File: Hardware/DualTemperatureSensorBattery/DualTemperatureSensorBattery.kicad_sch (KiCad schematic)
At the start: 22 parts, among them J2 Conn_01x06, Q101 BSS84, SW2 SW_Push, U1 ME54BS01_V1.0

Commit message: Rename the project. Finish routing.
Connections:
- net Enable-Battery: now also U1.8 (P1.06/AIN2); no longer U1.7 (P1.14/AIN7)
- net PROBE_1_DIVIDER: now also U1.4 (P1.11/AIN4); no longer U1.5 (P1.12/AIN5)
- net PROBE_2_DIVIDER: now also U1.5 (P1.12/AIN5); no longer U1.4 (P1.11/AIN4)
- net VDD: no longer J2.6 (Pin_6)
- net V_{BAT}: now also U1.7 (P1.14/AIN7); no longer U1.8 (P1.06/AIN2)
- net +BATT: now reaches BT1.1 (+), C6.1, JP1.1 (A), Probe3.1 (Pin_1)
- net +BATT: now also J2.6 (Pin_6)

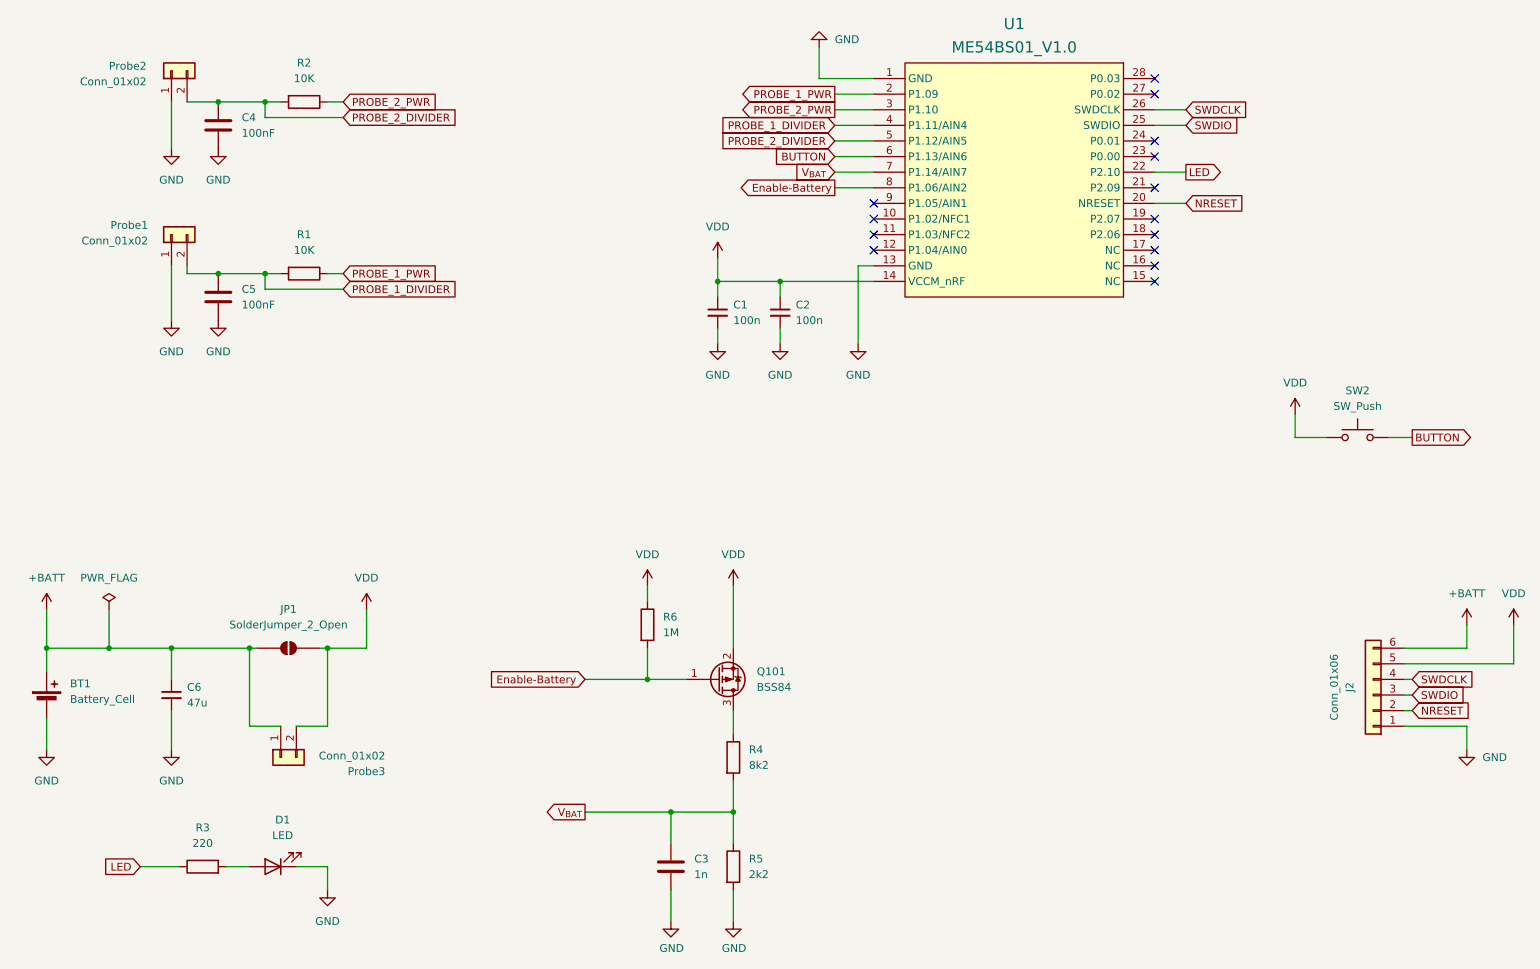
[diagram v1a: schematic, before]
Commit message: Removed the battery measurement. Reworked some of the layout.
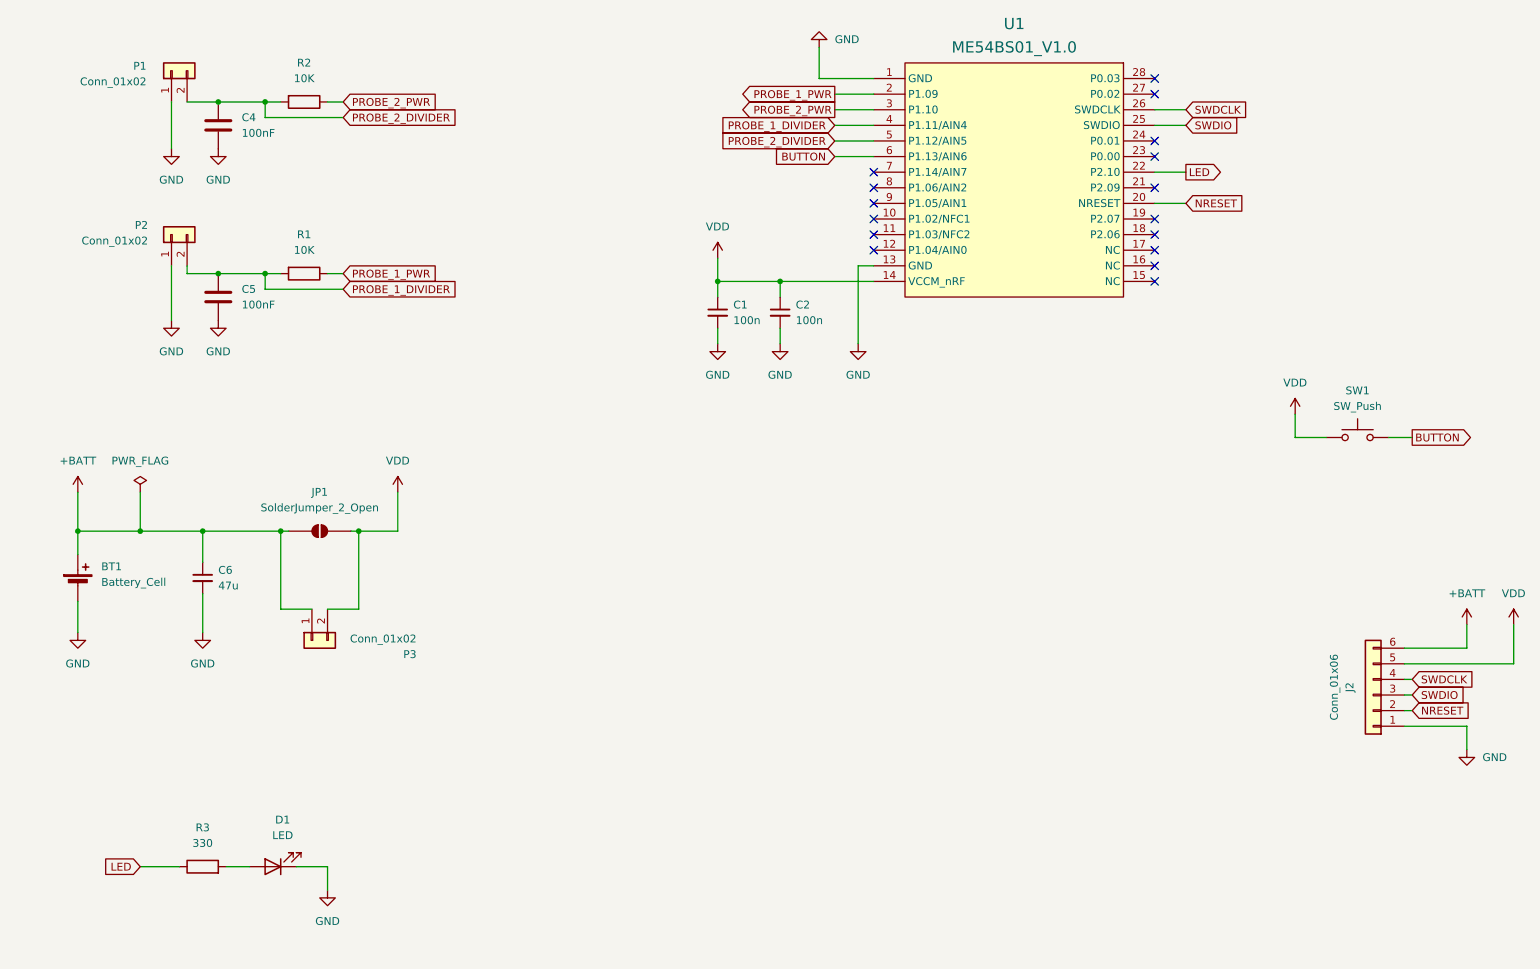
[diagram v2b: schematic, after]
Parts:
- removed C3: 1n, Resistor_SMD:R_0805_2012Metric, symbol Device:C
- removed Q101: BSS84, Package_TO_SOT_SMD:SOT-23-3, symbol Transistor_FET:BSS84
- removed R4: 8k2, Resistor_SMD:R_0805_2012Metric, symbol Device:R
- removed R5: 2k2, Resistor_SMD:R_0805_2012Metric, symbol Device:R
- removed R6: 1M, Resistor_SMD:R_0805_2012Metric, symbol Device:R
- R3: value 220 -> 330
- renumbered Probe2 to P1, Probe1 to P2, Probe3 to P3, SW2 to SW1
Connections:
- net Enable-Battery: no longer names the net of U1.8 (P1.06/AIN2)
- net V_{BAT}: no longer names the net of U1.7 (P1.14/AIN7)
- no-connect marks 14 -> 16
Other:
- moved on the sheet: BT1, C6, JP1, P3
